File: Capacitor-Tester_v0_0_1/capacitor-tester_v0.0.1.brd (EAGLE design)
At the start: 100 x 80 mm, 30 parts, among them IC1 AD8531ARZ, IC2 MC34063EBD-TR, J1 USB4125-GF-A-0190_REVA2, J2 DS1044-140G, J3 250-102, U1 AD5933, U2 LM6171AIMX/NOPB, Y1 LFSPXO018034

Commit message: v0.0.1 - Fix in the schematic. Bad label. Version before changing the input connector to Wago 250-103
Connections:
- removed net VOUT_2: J2.10, J2.11, J2.12, J2.13, J2.14, J2.8, J2.9, R7.1
- new net N$6: SJ1.2, SJ2.2, U1.8
- net MCLK: no longer SJ1.2, SJ2.2, U1.8
- net VIN: now also J2.10, J2.11, J2.12, J2.13, J2.14, J2.8, J2.9, R7.1
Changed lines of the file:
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@@
 <layer number="14" name="Route14" color="1" fill="6" visible="no" active="no"/>
 <layer number="15" name="Route15" color="4" fill="6" visible="no" active="no"/>
-<layer number="16" name="Bottom" color="1" fill="1" visible="yes" active="yes"/>
+<layer number="16" name="Bottom" color="1" fill="1" visible="no" active="yes"/>
 <layer number="17" name="Pads" color="2" fill="1" visible="yes" active="yes"/>
 <layer number="18" name="Vias" color="2" fill="1" visible="yes" active="yes"/>
@@
 <layer number="20" name="Dimension" color="24" fill="1" visible="yes" active="yes"/>
 <layer number="21" name="tPlace" color="7" fill="1" visible="yes" active="yes"/>
-<layer number="22" name="bPlace" color="7" fill="1" visible="yes" active="yes"/>
+<layer number="22" name="bPlace" color="7" fill="1" visible="no" active="yes"/>
 <layer number="23" name="tOrigins" color="15" fill="1" visible="yes" active="yes"/>
-<layer number="24" name="bOrigins" color="15" fill="1" visible="yes" active="yes"/>
+<layer number="24" name="bOrigins" color="15" fill="1" visible="no" active="yes"/>
 <layer number="25" name="tNames" color="7" fill="1" visible="yes" active="yes"/>
-<layer number="26" name="bNames" color="7" fill="1" visible="yes" active="yes"/>
+<layer number="26" name="bNames" color="7" fill="1" visible="no" active="yes"/>
 <layer number="27" name="tValues" color="7" fill="1" visible="no" active="yes"/>
 <layer number="28" name="bValues" color="7" fill="1" visible="no" active="yes"/>
@@
 <layer number="38" name="bTest" color="7" fill="1" visible="no" active="yes"/>
 <layer number="39" name="tKeepout" color="4" fill="11" visible="yes" active="yes"/>
-<layer number="40" name="bKeepout" color="1" fill="11" visible="yes" active="yes"/>
+<layer number="40" name="bKeepout" color="1" fill="11" visible="no" active="yes"/>
 <layer number="41" name="tRestrict" color="4" fill="10" visible="yes" active="yes"/>
-<layer number="42" name="bRestrict" color="1" fill="10" visible="yes" active="yes"/>
+<layer number="42" name="bRestrict" color="1" fill="10" visible="no" active="yes"/>
 <layer number="43" name="vRestrict" color="2" fill="10" visible="no" active="yes"/>
 <layer number="44" name="Drills" color="7" fill="1" visible="no" active="yes"/>
@@
 <layer number="49" name="Reference" color="7" fill="1" visible="no" active="yes"/>
 <layer number="51" name="tDocu" color="7" fill="1" visible="yes" active="yes"/>
-<layer number="52" name="bDocu" color="7" fill="1" visible="yes" active="yes"/>
+<layer number="52" name="bDocu" color="7" fill="1" visible="no" active="yes"/>
 <layer number="88" name="SimResults" color="9" fill="1" visible="no" active="no"/>
 <layer number="89" name="SimProbes" color="9" fill="1" visible="no" active="no"/>
@@
 <signal name="MCLK">
 <contactref element="Y1" pad="3"/>
-<contactref element="U1" pad="8"/>
-<contactref element="SJ1" pad="2"/>
-<contactref element="SJ2" pad="2"/>
 <contactref element="SJ1" pad="1"/>
-<wire x1="-5.53" y1="-68" x2="-5.53" y2="-73.4" width="0" layer="19" extent="1-1"/>
-<wire x1="-8.07" y1="-68" x2="-5.53" y2="-68" width="0" layer="19" extent="1-1"/>
-<wire x1="0" y1="-55.6" x2="-5.53" y2="-68" width="0" layer="19" extent="1-1"/>
-<wire x1="-7.01" y1="-17.25" x2="0" y2="-55.6" width="0" layer="19" extent="1-1"/>
+<wire x1="0" y1="-55.6" x2="-8.07" y2="-68" width="0" layer="19" extent="1-1"/>
 </signal>
 <signal name="FUNC_GEN">
@@
 <signal name="VIN">
 <contactref element="U1" pad="5"/>
+<contactref element="J2" pad="14"/>
+<contactref element="J2" pad="13"/>
+<contactref element="J2" pad="12"/>
+<contactref element="J2" pad="8"/>
+<contactref element="J2" pad="11"/>
+<contactref element="J2" pad="10"/>
+<contactref element="J2" pad="9"/>
+<contactref element="R7" pad="1"/>
+<wire x1="0" y1="-143.34" x2="-29.79" y2="-150.6" width="0" layer="19" extent="1-1"/>
+<wire x1="0" y1="-140.8" x2="0" y2="-143.34" width="0" layer="19" extent="1-1"/>
+<wire x1="0" y1="-138.26" x2="0" y2="-140.8" width="0" layer="19" extent="1-1"/>
+<wire x1="0" y1="-135.72" x2="0" y2="-138.26" width="0" layer="19" extent="1-1"/>
+<wire x1="0" y1="-133.18" x2="0" y2="-135.72" width="0" layer="19" extent="1-1"/>
+<wire x1="0" y1="-130.64" x2="0" y2="-133.18" width="0" layer="19" extent="1-1"/>
+<wire x1="0" y1="-128.1" x2="0" y2="-130.64" width="0" layer="19" extent="1-1"/>
+<wire x1="-7.01" y1="-15.3" x2="0" y2="-128.1" width="0" layer="19" extent="1-1"/>
 </signal>
 <signal name="VOUT">
@@
 <wire x1="-5.424" y1="-108.945" x2="-18.65" y2="-115.2" width="0" layer="19" extent="1-1"/>
 </signal>
-<signal name="VOUT_2">
-<contactref element="J2" pad="14"/>
-<contactref element="J2" pad="13"/>
-<contactref element="J2" pad="12"/>
-<contactref element="J2" pad="8"/>
-<contactref element="J2" pad="11"/>
-<contactref element="J2" pad="10"/>
-<contactref element="J2" pad="9"/>
-<contactref element="R7" pad="1"/>
-<wire x1="0" y1="-143.34" x2="-29.79" y2="-150.6" width="0" layer="19" extent="1-1"/>
-<wire x1="0" y1="-140.8" x2="0" y2="-143.34" width="0" layer="19" extent="1-1"/>
-<wire x1="0" y1="-138.26" x2="0" y2="-140.8" width="0" layer="19" extent="1-1"/>
-<wire x1="0" y1="-135.72" x2="0" y2="-138.26" width="0" layer="19" extent="1-1"/>
-<wire x1="0" y1="-133.18" x2="0" y2="-135.72" width="0" layer="19" extent="1-1"/>
-<wire x1="0" y1="-130.64" x2="0" y2="-133.18" width="0" layer="19" extent="1-1"/>
-<wire x1="0" y1="-128.1" x2="0" y2="-130.64" width="0" layer="19" extent="1-1"/>
-</signal>
 <signal name="N$2">
 <contactref element="U2" pad="2"/>
@@
 <wire x1="0" y1="-164.57" x2="-37.15" y2="-180" width="0" layer="19" extent="1-1"/>
 </signal>
+<signal name="N$6">
+<contactref element="SJ1" pad="2"/>
+<contactref element="SJ2" pad="2"/>
+<contactref element="U1" pad="8"/>
+<wire x1="-5.53" y1="-68" x2="-5.53" y2="-73.4" width="0" layer="19" extent="1-1"/>
+<wire x1="-7.01" y1="-17.25" x2="-5.53" y2="-68" width="0" layer="19" extent="1-1"/>
+</signal>
 </signals>

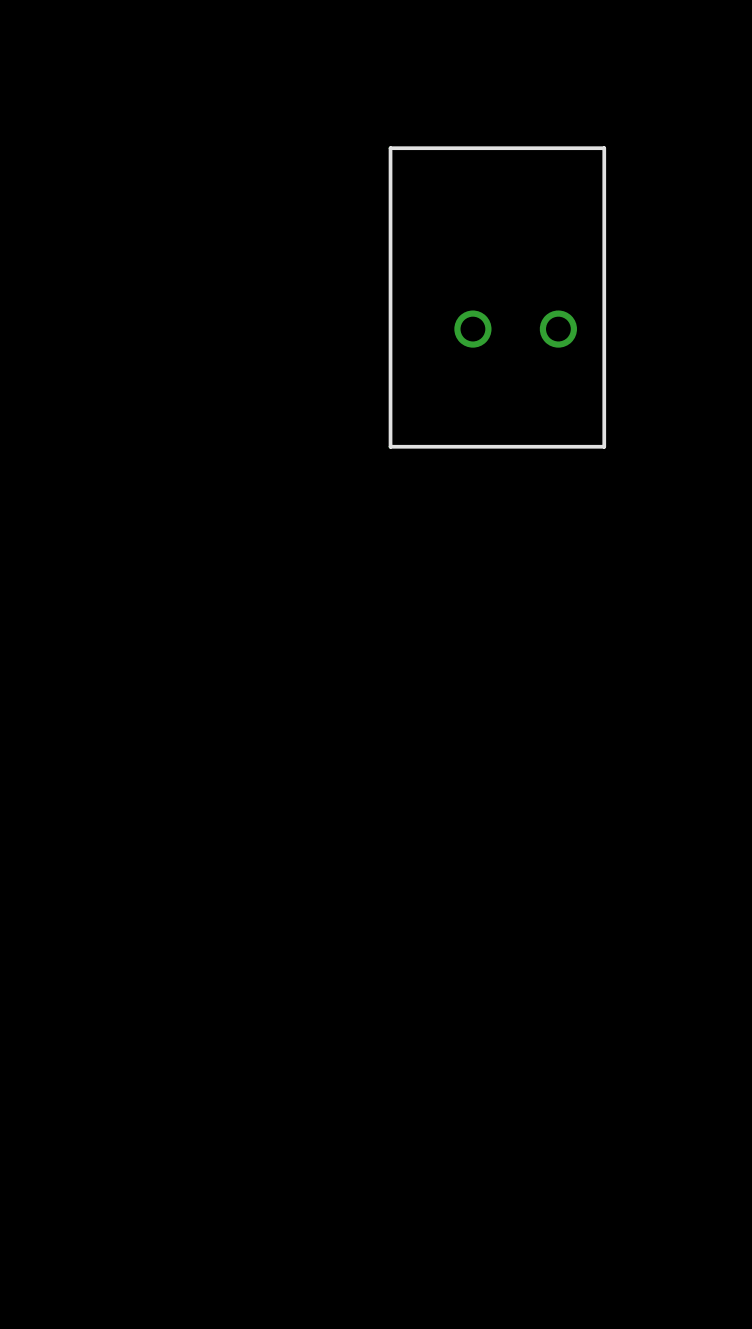
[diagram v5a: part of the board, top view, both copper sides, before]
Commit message: v0.0.1 - Changed wago 250-102 for 250-103 and connected FUNC_GEN to the input connector
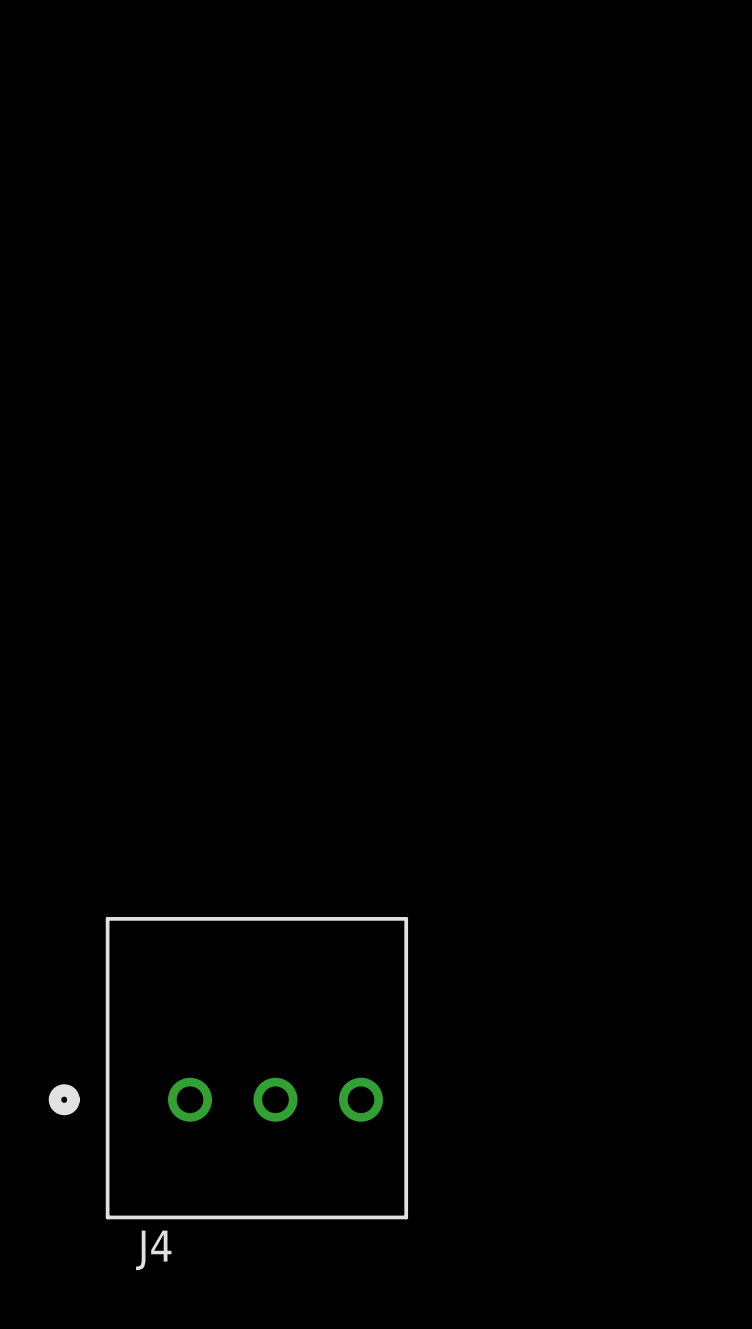
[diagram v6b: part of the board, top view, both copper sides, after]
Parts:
- removed J3: 250-102, custom_library:CONN_250-102_WAG
- added J4: 250-103, custom_library:CONN3_250-103_WAG
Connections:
- net FUNC_GEN: now also J4.3
- net SCL: now also J4.2; no longer J3.2
- net SDA: now also J4.1; no longer J3.1
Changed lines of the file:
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@@
 <attribute name="VALUE" x="-75.835" y="-197.305" size="1.27" layer="27"/>
 </element>
-<element name="J3" library="custom_library" package="CONN_250-102_WAG" value="250-102" x="-90.8" y="-175.2" smashed="yes">
-<attribute name="COPYRIGHT" value="Copyright (C) 2024 Ultra Librarian. All rights reserved." x="-90.8" y="-175.2" size="1.778" layer="27" display="off"/>
-<attribute name="MANUFACTURER_PART_NUMBER" value="250-102" x="-90.8" y="-175.2" size="1.778" layer="27" display="off"/>
-<attribute name="MFR_NAME" value="Wago" x="-90.8" y="-175.2" size="1.778" layer="27" display="off"/>
-<attribute name="NAME" x="-93.0606" y="-175.835" size="1.27" layer="27" ratio="6" rot="SR0"/>
-<attribute name="VALUE" x="-91.5366" y="-175.835" size="1.27" layer="27" ratio="6" rot="SR0"/>
+<element name="J4" library="custom_library" package="CONN3_250-103_WAG" value="250-103" x="-102.4" y="-206.8" smashed="yes">
+<attribute name="COPYRIGHT" value="Copyright (C) 2025 Ultra Librarian. All rights reserved." x="-102.4" y="-206.8" size="1.778" layer="27" display="off"/>
+<attribute name="MANUFACTURER_PART_NUMBER" value="250-103" x="-102.4" y="-206.8" size="1.778" layer="27" display="off"/>
+<attribute name="MFR_NAME" value="Wago" x="-102.4" y="-206.8" size="1.778" layer="27" display="off"/>
+<attribute name="NAME" x="-104.5334" y="-213.435" size="1.27" layer="25" ratio="6" rot="SR0"/>
 </element>
 </elements>
@@
 <contactref element="U1" pad="16"/>
 <contactref element="R1" pad="1"/>
-<contactref element="J3" pad="2"/>
+<contactref element="J4" pad="2"/>
 <wire x1="0" y1="-12.7" x2="-11.99" y2="-86.8" width="0" layer="19" extent="1-1"/>
-<wire x1="-87.2948" y1="-175.2" x2="-11.99" y2="-86.8" width="0" layer="19" extent="1-1"/>
+<wire x1="-98.8948" y1="-206.8" x2="-11.99" y2="-86.8" width="0" layer="19" extent="1-1"/>
 </signal>
 <signal name="SDA">
 <contactref element="U1" pad="15"/>
 <contactref element="R3" pad="1"/>
-<contactref element="J3" pad="1"/>
+<contactref element="J4" pad="1"/>
 <wire x1="0" y1="-13.35" x2="-7.99" y2="-86.8" width="0" layer="19" extent="1-1"/>
-<wire x1="-90.8" y1="-175.2" x2="-7.99" y2="-86.8" width="0" layer="19" extent="1-1"/>
+<wire x1="-102.4" y1="-206.8" x2="-7.99" y2="-86.8" width="0" layer="19" extent="1-1"/>
 </signal>
 <signal name="MCLK">
@@
 <signal name="FUNC_GEN">
 <contactref element="SJ2" pad="1"/>
+<contactref element="J4" pad="3"/>
+<wire x1="-95.3896" y1="-206.8" x2="-8.07" y2="-73.4" width="0" layer="19" extent="1-1"/>
 </signal>
 <signal name="RFB">
